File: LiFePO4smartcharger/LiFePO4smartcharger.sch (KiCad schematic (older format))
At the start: 100 parts, among them J1 Conn_01x02, J10 Conn_01x01, J11 Conn_01x01, J12 Conn_01x04, J13 Conn_01x01, J2 Conn_02x03_Odd_Even, J3 Conn_01x02, J4 Conn_01x02, J5 Barrel_Jack, J6 Conn_01x01, J7 Conn_01x01, J8 Conn_01x02, J9 Conn_01x02, Q1 TIP42, Q2 TIP41, Q3 2N3906, Q4 TIP41C, T1 Transformer_1P1Sdotted, U1 ATMEGA328P-PU, U2 LM358, U3 LCD-016N002L, U4 TL494, U9 LM7805_TO220, X3 16MHz

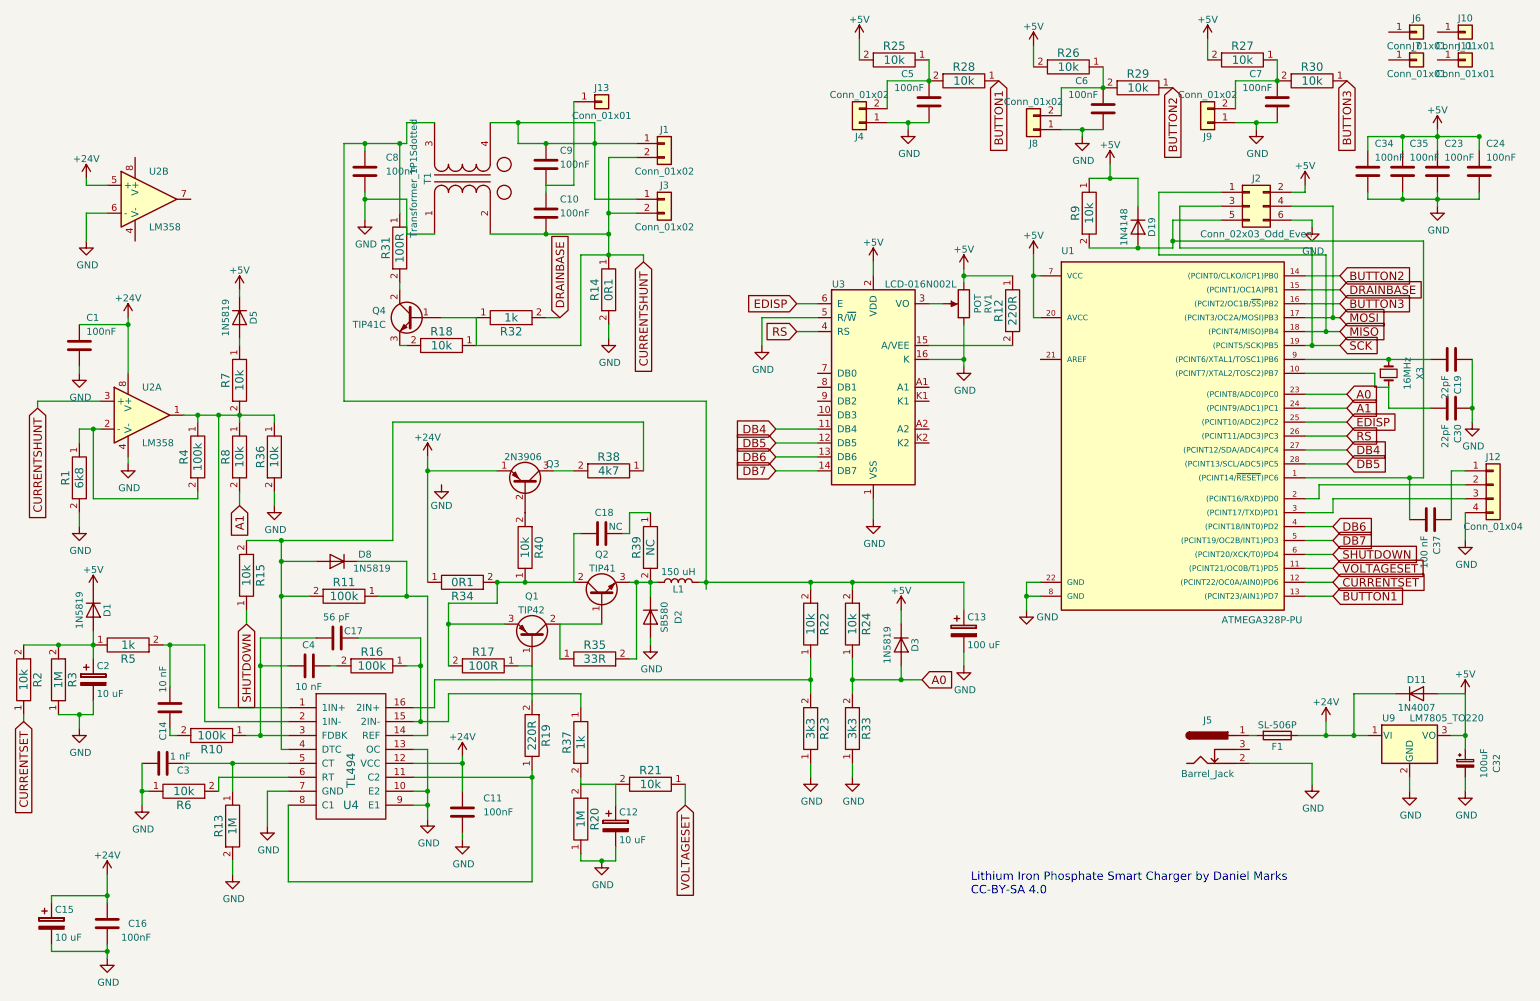
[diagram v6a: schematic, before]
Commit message: Added compensation for shunt resistor voltage drop
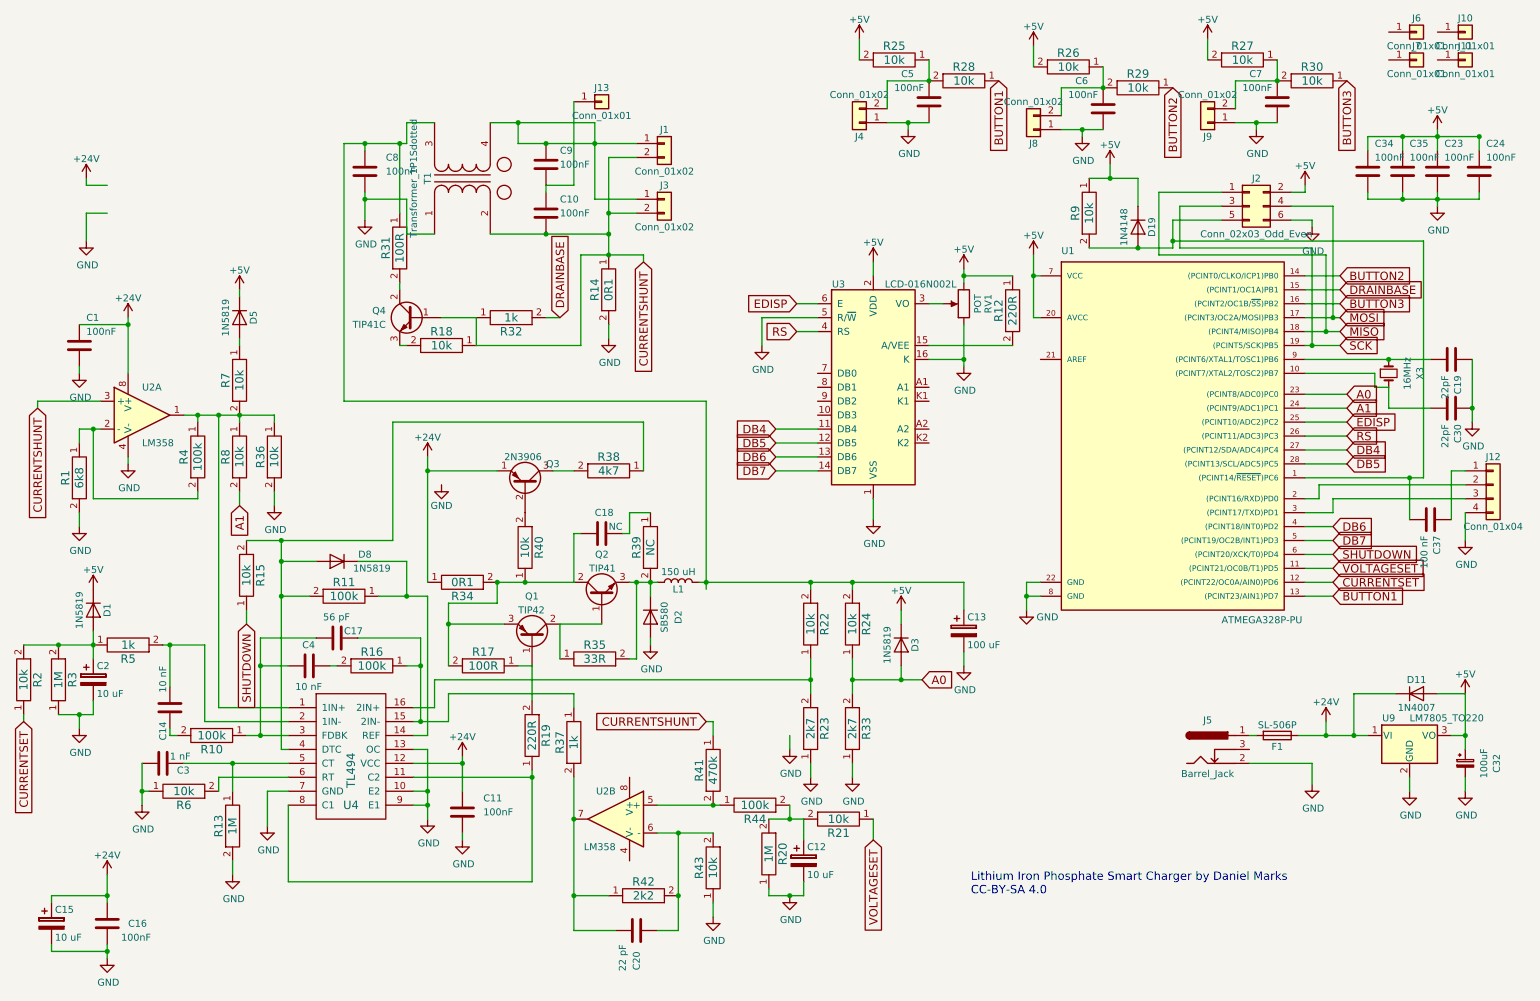
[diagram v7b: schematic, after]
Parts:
- added C20: 22 pF, Capacitors_THT:C_Disc_D5.0mm_W2.5mm_P5.00mm, symbol C
- added R41: 470k, Resistors_THT:R_Axial_DIN0207_L6.3mm_D2.5mm_P7.62mm_Horizontal, symbol RES
- added R42: 2k2, Resistors_THT:R_Axial_DIN0207_L6.3mm_D2.5mm_P7.62mm_Horizontal, symbol RES
- added R43: 10k, Resistors_THT:R_Axial_DIN0207_L6.3mm_D2.5mm_P7.62mm_Horizontal, symbol RES
- added R44: 100k, Resistors_THT:R_Axial_DIN0207_L6.3mm_D2.5mm_P7.62mm_Horizontal, symbol RES
- R23, R33: value 3k3 -> 2k7
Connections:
- net +24V: no longer U2.5 (+)
- net CURRENTSHUNT: now also R41.1
- net GND: now also R43.1; no longer U2.6 (-)
- net at C12.1, R20.2, R21.2: now also R44.2; no longer R37.2
- net at U2.7: now also R37.2, C20.2, R42.1
- new net: R41.2, R44.1, U2.5 (+)
- new net: C20.1, R42.2, R43.2, U2.6 (-)
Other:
- moved on the sheet: C12, R20, R21, R37, U2B

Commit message: JLCPCB 2021-03-26
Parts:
- removed J5: Barrel_Jack, Connectors:BARREL_JACK, symbol Barrel_Jack
- added J14, J5: Conn_01x02, Connectors_Terminal_Blocks:TerminalBlock_bornier-2_P5.08mm, symbol Conn_01x02
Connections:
- net GND: now also J5.2 (Pin_2)
- net at F1.2: now also J5.1 (Pin_1)
- net at R31.2: now also J14.1 (Pin_1); no longer Q4.2 (C)
- new net: J14.2 (Pin_2), Q4.2 (C)
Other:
- moved on the sheet: Q4, R18, R31, R32
